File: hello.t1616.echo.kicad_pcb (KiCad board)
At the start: 2 copper layers, 51.4 x 25.4 mm, 10 parts, among them J1 Conn_01x03_Male, J2 Conn_FTDI_01x06_Male, SW1 BUTTON_B3SN, U1 ATtiny1616-S

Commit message: Finished (?) board
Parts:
- removed D1: LED YLW, fab:LED_1206
- removed D2: LED GRN, fab:LED_1206
- removed R1, R2, R3: 1K, fab:R_1206
- removed SW1: BUTTON_B3SN, fab:Button_Omron_B3SN_6x6mm
- J1: footprint Connector_PinHeader_2.54mm:PinHeader_1x03_P2.54mm_Horizontal -> fab:Header_SMD_01x03_P2.54mm_Horizontal_Male
- J2: footprint Connector_PinHeader_2.54mm:PinHeader_1x06_P2.54mm_Vertical -> fab:Header_SMD_01x06_P2.54mm_Horizontal_Male
- moved J1 16.2 mm to (131.4, 121.3)
- moved J2 3.81 mm to (158.1, 111.8)
- moved C1 1.27 mm to (136.5, 117.5)
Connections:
- J2 pad 2: Net-(J2-Pad2) -> (no net)
- J2 pad 6: Net-(J2-Pad6) -> (no net)
- U1 pad 10: Net-(U1-Pad10) -> (no net)
- U1 pad 11: Net-(U1-Pad11) -> (no net)
- U1 pad 12: Net-(U1-Pad12) -> (no net)
- U1 pad 13: Net-(U1-Pad13) -> (no net)
- U1 pad 14: Net-(U1-Pad14) -> (no net)
- U1 pad 15: Net-(U1-Pad15) -> (no net)
- U1 pad 17: RX -> (no net)
- U1 pad 18: TX -> (no net)
- U1 pad 19: Net-(R1-Pad1) -> (no net)
- U1 pad 2: Net-(U1-Pad2) -> (no net)
- U1 pad 3: LED1 -> (no net)
- U1 pad 4: LED2 -> (no net)
- U1 pad 5: Net-(U1-Pad5) -> (no net)
- U1 pad 6: Net-(U1-Pad6) -> (no net)
- U1 pad 7: Net-(U1-Pad7) -> (no net)
- U1 pad 8: Net-(U1-Pad8) -> TX
- U1 pad 9: Net-(U1-Pad9) -> RX
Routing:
- net GND: track 115.4 -> 35.6 mm
- net VCC: track 70.7 -> 32.7 mm
- net Net-(R1-Pad1): track 32.1 -> 0.00 mm
- net RX: track 40.6 -> 10.9 mm
- net Net-(J1-Pad3): track 44.0 -> 18.0 mm
- net TX: track 36.4 -> 12.8 mm
- net LED1: track 13.1 -> 0.00 mm
- net LED2: track 5.22 -> 0.00 mm
- net Net-(D2-Pad2): track 3.81 -> 0.00 mm
- net Net-(D1-Pad2): track 3.81 -> 0.00 mm
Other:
- board size 51.4 x 25.4 mm -> 36.2 x 17.8 mm
- board text added: "GND"
- board text added: "UPDI"
- board text added: "VCC"

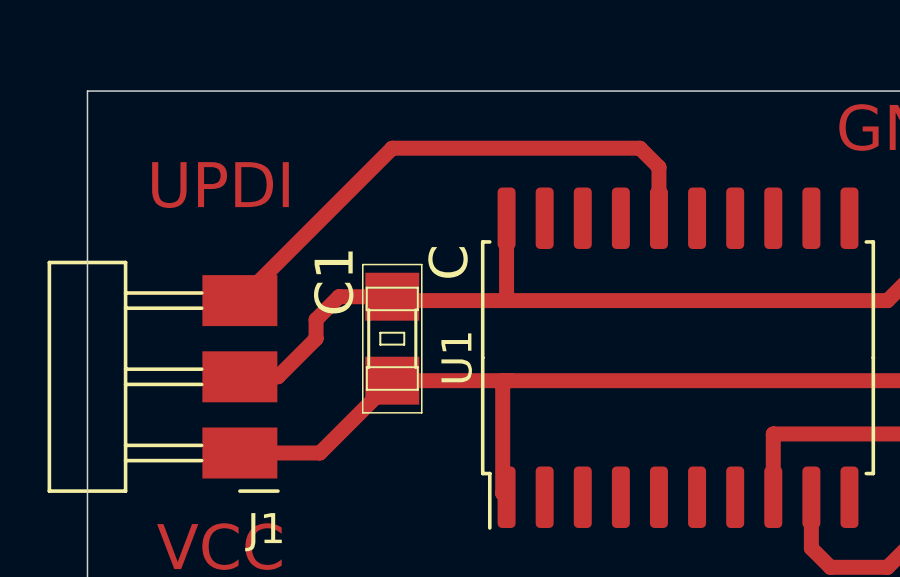
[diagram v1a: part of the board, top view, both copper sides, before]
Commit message: Surface mount headers, added README.
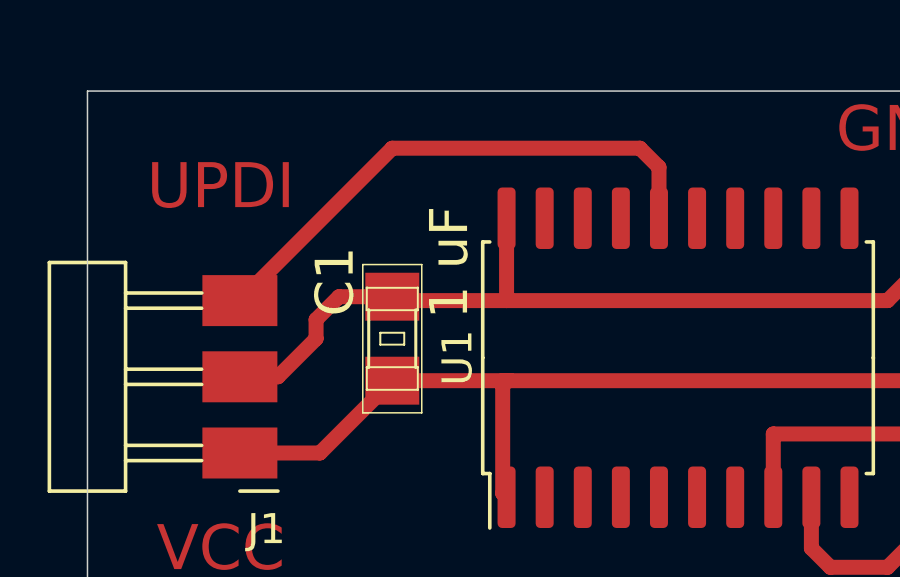
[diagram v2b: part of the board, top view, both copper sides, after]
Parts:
- C1: value C -> 1 uF
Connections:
- net Net-(J1-Pad3) renamed /UPDI
- J2 pad 2: (no net) -> Net-(J2-Pad2)
- J2 pad 6: (no net) -> Net-(J2-Pad6)
- U1 pad 10: (no net) -> Net-(U1-Pad10)
- U1 pad 11: (no net) -> Net-(U1-Pad11)
- U1 pad 12: (no net) -> Net-(U1-Pad12)
- U1 pad 13: (no net) -> Net-(U1-Pad13)
- U1 pad 14: (no net) -> Net-(U1-Pad14)
- U1 pad 15: (no net) -> Net-(U1-Pad15)
- U1 pad 17: (no net) -> Net-(U1-Pad17)
- U1 pad 18: (no net) -> Net-(U1-Pad18)
- U1 pad 19: (no net) -> Net-(U1-Pad19)
- U1 pad 2: (no net) -> Net-(U1-Pad2)
- U1 pad 3: (no net) -> Net-(U1-Pad3)
- U1 pad 4: (no net) -> Net-(U1-Pad4)
- U1 pad 5: (no net) -> Net-(U1-Pad5)
- U1 pad 6: (no net) -> Net-(U1-Pad6)
- U1 pad 7: (no net) -> Net-(U1-Pad7)
